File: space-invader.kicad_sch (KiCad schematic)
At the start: 35 parts, among them SW1 SW_Push, SW10 SW_Push, SW11 SW_Push, SW12 SW_Push, SW13 SW_Push, SW14 SW_Push, SW15 SW_Push, SW16 SW_Push, SW17 SW_Push, SW2 SW_Push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

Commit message: there be graphics
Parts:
- U1: footprint PCM_marbastlib-xp-promicroish:Xiao_nRF52840_ACH -> PCM_marbastlib-xp-promicroish:Xiao_nRF52840_AC_Reflow
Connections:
- net col0: now also U1.11 (P1.15); no longer U1.12 (P1.14)
- net col1: now also U1.12 (P1.14); no longer U1.13 (P1.13)
- net col2: now also U1.7 (P1.11); no longer U1.6 (P0.05)
- net row0: now also U1.13 (P1.13); no longer U1.4 (P0.29)
- net row1: now also U1.14 (P1.12); no longer U1.5 (P0.04)
- net row2: now also U1.6 (P0.05); no longer U1.7 (P1.11)
- no-connect marks 0 -> 11
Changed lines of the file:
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@@
 		(color 0 0 0 0)
 	)
+	(no_connect
+		(at 138.43 24.13)
+	)
+	(no_connect
+		(at 140.97 57.15)
+	)
+	(no_connect
+		(at 130.81 24.13)
+	)
+	(no_connect
+		(at 138.43 57.15)
+	)
+	(no_connect
+		(at 133.35 24.13)
+	)
+	(no_connect
+		(at 120.65 39.37)
+	)
+	(no_connect
+		(at 135.89 24.13)
+	)
+	(no_connect
+		(at 120.65 36.83)
+	)
+	(no_connect
+		(at 146.05 34.29)
+	)
+	(no_connect
+		(at 146.05 29.21)
+	)
+	(no_connect
+		(at 146.05 31.75)
+	)
 	(wire
 		(pts
@@
 	(global_label "col1"
 		(shape input)
+		(at 146.05 39.37 0)
+		(fields_autoplaced yes)
+		(effects
+			(font
+				(size 1.27 1.27)
+			)
+			(justify left)
+		)
+		(property "Intersheetrefs" "${INTERSHEET_REFS}"
+			(at 153.1475 39.37 0)
+			(effects
+				(font
+					(size 1.27 1.27)
+				)
+				(justify left)
+				(hide yes)
+			)
+		)
+	)
+	(global_label "col0"
+		(shape input)
+		(at 146.05 36.83 0)
+		(fields_autoplaced yes)
+		(effects
+			(font
+				(size 1.27 1.27)
+			)
+			(justify left)
+		)
+		(property "Intersheetrefs" "${INTERSHEET_REFS}"
+			(at 153.1475 36.83 0)
+			(effects
+				(font
+					(size 1.27 1.27)
+				)
+				(justify left)
+				(hide yes)
+			)
+		)
+	)
+	(global_label "row0"
+		(shape input)
 		(at 146.05 41.91 0)
 		(fields_autoplaced yes)
@@
 		)
 		(property "Intersheetrefs" "${INTERSHEET_REFS}"
-			(at 153.1475 41.91 0)
+			(at 153.5104 41.91 0)
 			(effects
 				(font
@@
 		)
 	)
-	(global_label "col0"
-		(shape input)
-		(at 146.05 39.37 0)
+	(global_label "col4"
+		(shape input)
+		(at 90.17 21.59 90)
 		(fields_autoplaced yes)
 		(effects
@@
 		)
 		(property "Intersheetrefs" "${INTERSHEET_REFS}"
-			(at 153.1475 39.37 0)
+			(at 90.17 14.4925 90)
 			(effects
 				(font
@@
 		)
 	)
-	(global_label "row0"
-		(shape input)
-		(at 120.65 36.83 180)
+	(global_label "row2"
+		(shape input)
+		(at 120.65 41.91 180)
 		(fields_autoplaced yes)
 		(effects
@@
 		)
 		(property "Intersheetrefs" "${INTERSHEET_REFS}"
-			(at 113.1896 36.83 0)
+			(at 113.1896 41.91 0)
+			(effects
+				(font
+					(size 1.27 1.27)
+				)
+				(justify right)
+				(hide yes)
+			)
+		)
+	)
+	(global_label "row1"
+		(shape input)
+		(at 146.05 44.45 0)
+		(fields_autoplaced yes)
+		(effects
+			(font
+				(size 1.27 1.27)
+			)
+			(justify left)
+		)
+		(property "Intersheetrefs" "${INTERSHEET_REFS}"
+			(at 153.5104 44.45 0)
+			(effects
+				(font
+					(size 1.27 1.27)
+				)
+				(justify left)
+				(hide yes)
+			)
+		)
+	)
+	(global_label "row1"
+		(shape input)
+		(at 33.02 52.07 180)
+		(fields_autoplaced yes)
+		(effects
+			(font
+				(size 1.27 1.27)
+			)
+			(justify right)
+		)
+		(property "Intersheetrefs" "${INTERSHEET_REFS}"
+			(at 25.5596 52.07 0)
 			(effects
 				(font
@@
 	(global_label "col4"
 		(shape input)
-		(at 90.17 21.59 90)
-		(fields_autoplaced yes)
-		(effects
-			(font
-				(size 1.27 1.27)
-			)
-			(justify left)
-		)
-		(property "Intersheetrefs" "${INTERSHEET_REFS}"
-			(at 90.17 14.4925 90)
-			(effects
-				(font
-					(size 1.27 1.27)
-				)
-				(justify left)
-				(hide yes)
-			)
-		)
-	)
-	(global_label "row2"
+		(at 120.65 31.75 180)
+		(fields_autoplaced yes)
+		(effects
+			(font
+				(size 1.27 1.27)
+			)
+			(justify right)
+		)
+		(property "Intersheetrefs" "${INTERSHEET_REFS}"
+			(at 113.5525 31.75 0)
+			(effects
+				(font
+					(size 1.27 1.27)
+				)
+				(justify right)
+				(hide yes)
+			)
+		)
+	)
+	(global_label "col2"
 		(shape input)
 		(at 120.65 44.45 180)
@@
 		)
 		(property "Intersheetrefs" "${INTERSHEET_REFS}"
-			(at 113.1896 44.45 0)
-			(effects
-				(font
-					(size 1.27 1.27)
-				)
-				(justify right)
-				(hide yes)
-			)
-		)
-	)
-	(global_label "row1"
-		(shape input)
-		(at 120.65 39.37 180)
-		(fields_autoplaced yes)
-		(effects
-			(font
-				(size 1.27 1.27)
-			)
-			(justify right)
-		)
-		(property "Intersheetrefs" "${INTERSHEET_REFS}"
-			(at 113.1896 39.37 0)
-			(effects
-				(font
-					(size 1.27 1.27)
-				)
-				(justify right)
-				(hide yes)
-			)
-		)
-	)
-	(global_label "row1"
-		(shape input)
-		(at 33.02 52.07 180)
-		(fields_autoplaced yes)
-		(effects
-			(font
-				(size 1.27 1.27)
-			)
-			(justify right)
-		)
-		(property "Intersheetrefs" "${INTERSHEET_REFS}"
-			(at 25.5596 52.07 0)
-			(effects
-				(font
-					(size 1.27 1.27)
-				)
-				(justify right)
-				(hide yes)
-			)
-		)
-	)
-	(global_label "col4"
-		(shape input)
-		(at 120.65 31.75 180)
-		(fields_autoplaced yes)
-		(effects
-			(font
-				(size 1.27 1.27)
-			)
-			(justify right)
-		)
-		(property "Intersheetrefs" "${INTERSHEET_REFS}"
-			(at 113.5525 31.75 0)
-			(effects
-				(font
-					(size 1.27 1.27)
-				)
-				(justify right)
-				(hide yes)
-			)
-		)
-	)
-	(global_label "col2"
-		(shape input)
-		(at 120.65 41.91 180)
-		(fields_autoplaced yes)
-		(effects
-			(font
-				(size 1.27 1.27)
-			)
-			(justify right)
-		)
-		(property "Intersheetrefs" "${INTERSHEET_REFS}"
-			(at 113.5525 41.91 0)
+			(at 113.5525 44.45 0)
 			(effects
 				(font
@@
 			)
 		)
-		(property "Footprint" "PCM_marbastlib-xp-promicroish:Xiao_nRF52840_ACH"
+		(property "Footprint" "PCM_marbastlib-xp-promicroish:Xiao_nRF52840_AC_Reflow"
 			(at 133.35 73.66 0)
 			(effects

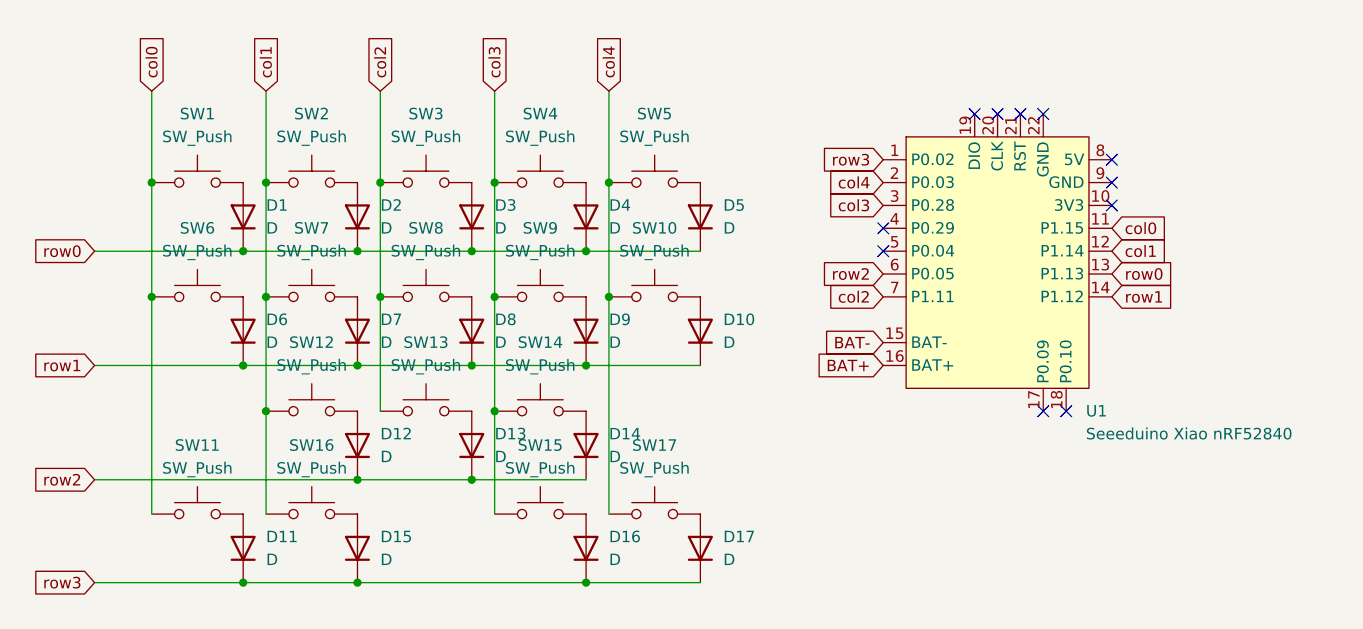
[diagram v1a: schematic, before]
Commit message: flipped XIAO upside down
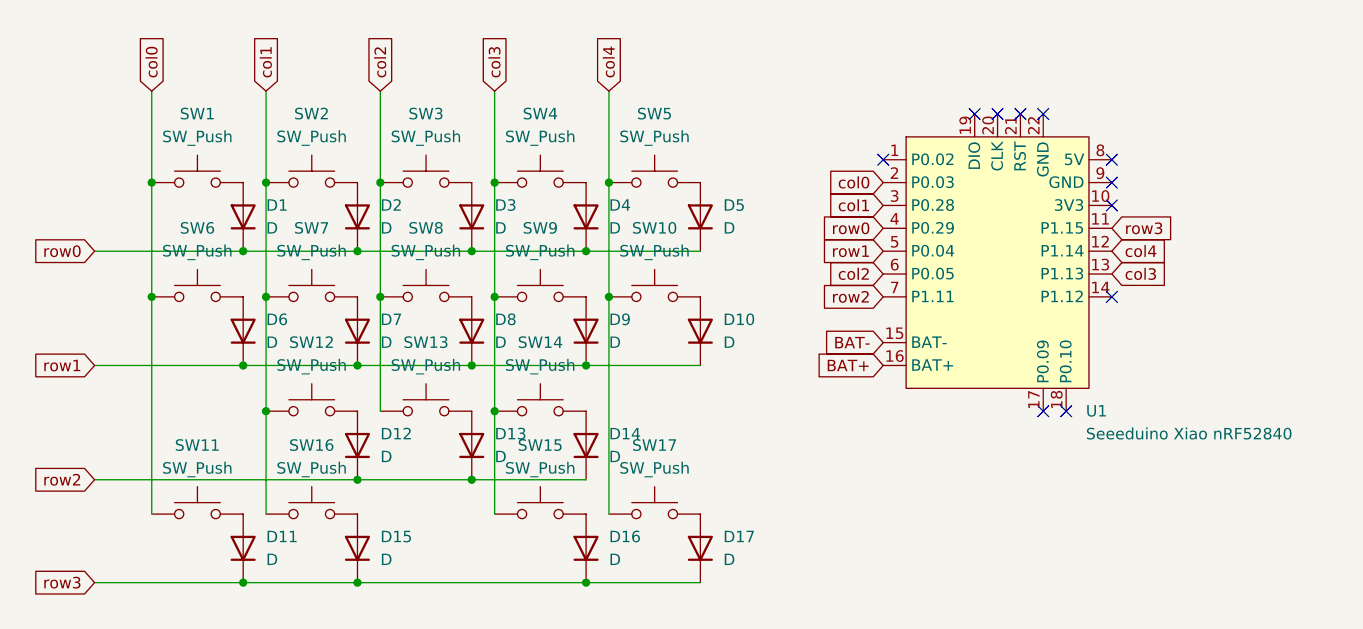
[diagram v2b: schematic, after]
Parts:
- U1: footprint PCM_marbastlib-xp-promicroish:Xiao_nRF52840_AC_Reflow -> PCM_marbastlib-xp-promicroish:Xiao_nRF52840_AC_Reflow_invert
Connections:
- net col0: now also U1.2 (P0.03); no longer U1.11 (P1.15)
- net col1: now also U1.3 (P0.28); no longer U1.12 (P1.14)
- net col2: now also U1.6 (P0.05); no longer U1.7 (P1.11)
- net col3: now also U1.13 (P1.13); no longer U1.3 (P0.28)
- net col4: now also U1.12 (P1.14); no longer U1.2 (P0.03)
- net row0: now also U1.4 (P0.29); no longer U1.13 (P1.13)
- net row1: now also U1.5 (P0.04); no longer U1.14 (P1.12)
- net row2: now also U1.7 (P1.11); no longer U1.6 (P0.05)
- net row3: now also U1.11 (P1.15); no longer U1.1 (P0.02)

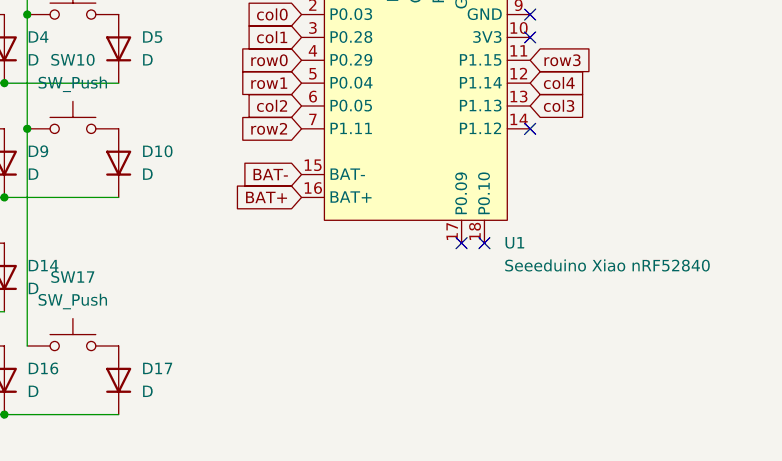
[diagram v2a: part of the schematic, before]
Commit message: added on-off switch
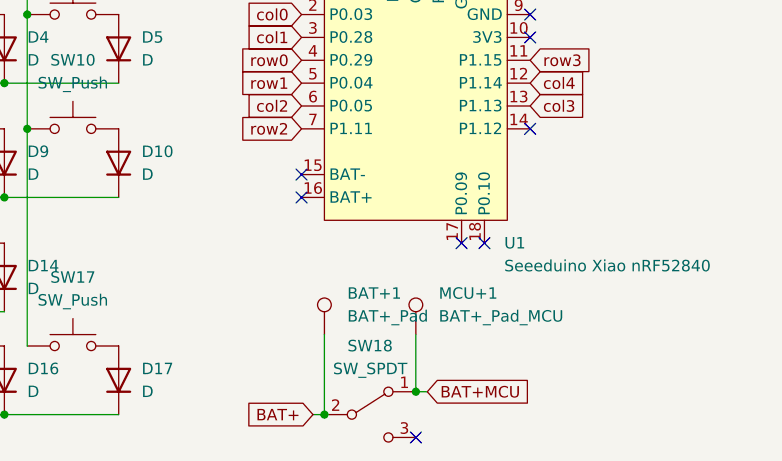
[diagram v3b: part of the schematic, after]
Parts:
- added BAT+1: BAT+_Pad, TestPoint:TestPoint_Pad_1.5x1.5mm, symbol Connector:TestPoint
- added MCU+1: BAT+_Pad_MCU, TestPoint:TestPoint_Pad_1.5x1.5mm, symbol Connector:TestPoint
- added SW18: SW_SPDT, PCM_marbastlib-various:SW_MSK12C02-HB, symbol Switch:SW_SPDT
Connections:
- net BAT+: now also BAT+1.1, SW18.2 (B); no longer U1.16 (BAT+)
- net BAT-: no longer names the net of U1.15 (BAT-)
- new net BAT+MCU: MCU+1.1, SW18.1 (A)
- no-connect marks 11 -> 14
